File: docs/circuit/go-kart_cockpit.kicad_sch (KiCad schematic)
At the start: 21 parts, among them J1 2x13, J2 2x13, Q1 TIP120, SW1 SW_MEC_5E, X1 AVR-ISP-10, X2 Display (2x3 male), X3 24V Hupe, X4 Start/Stop/Rückwärts, X5 Bluetooth-Modul, X6 Taster rechts (2x5 male), X7 Taster links (male)

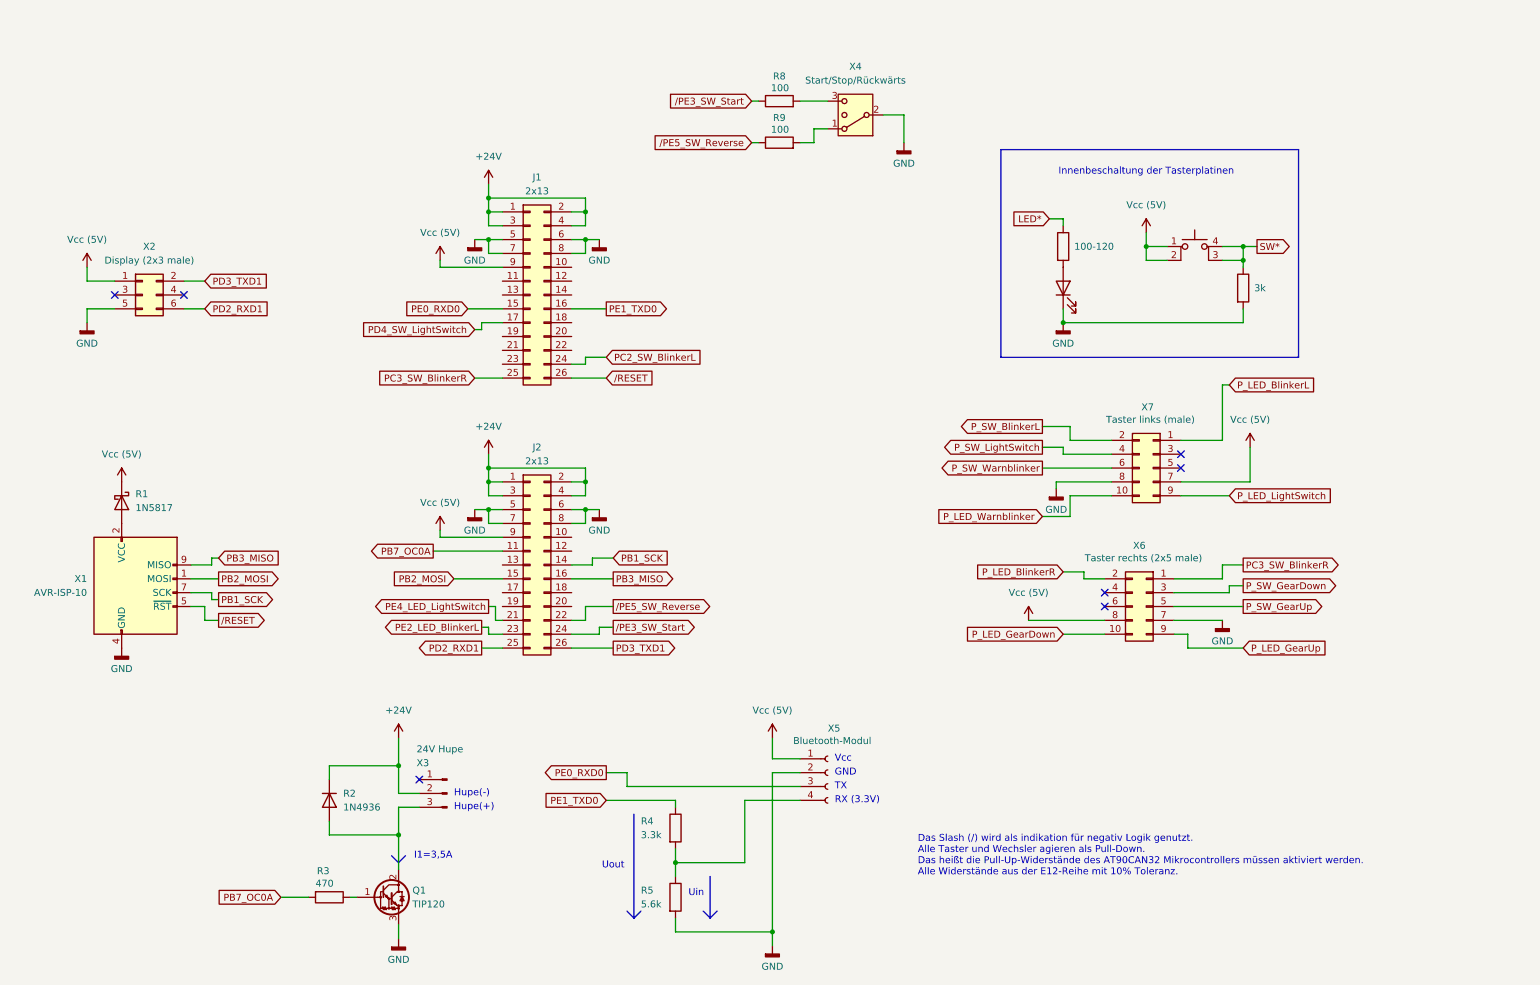
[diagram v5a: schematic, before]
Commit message: feat: planned connections to MCU
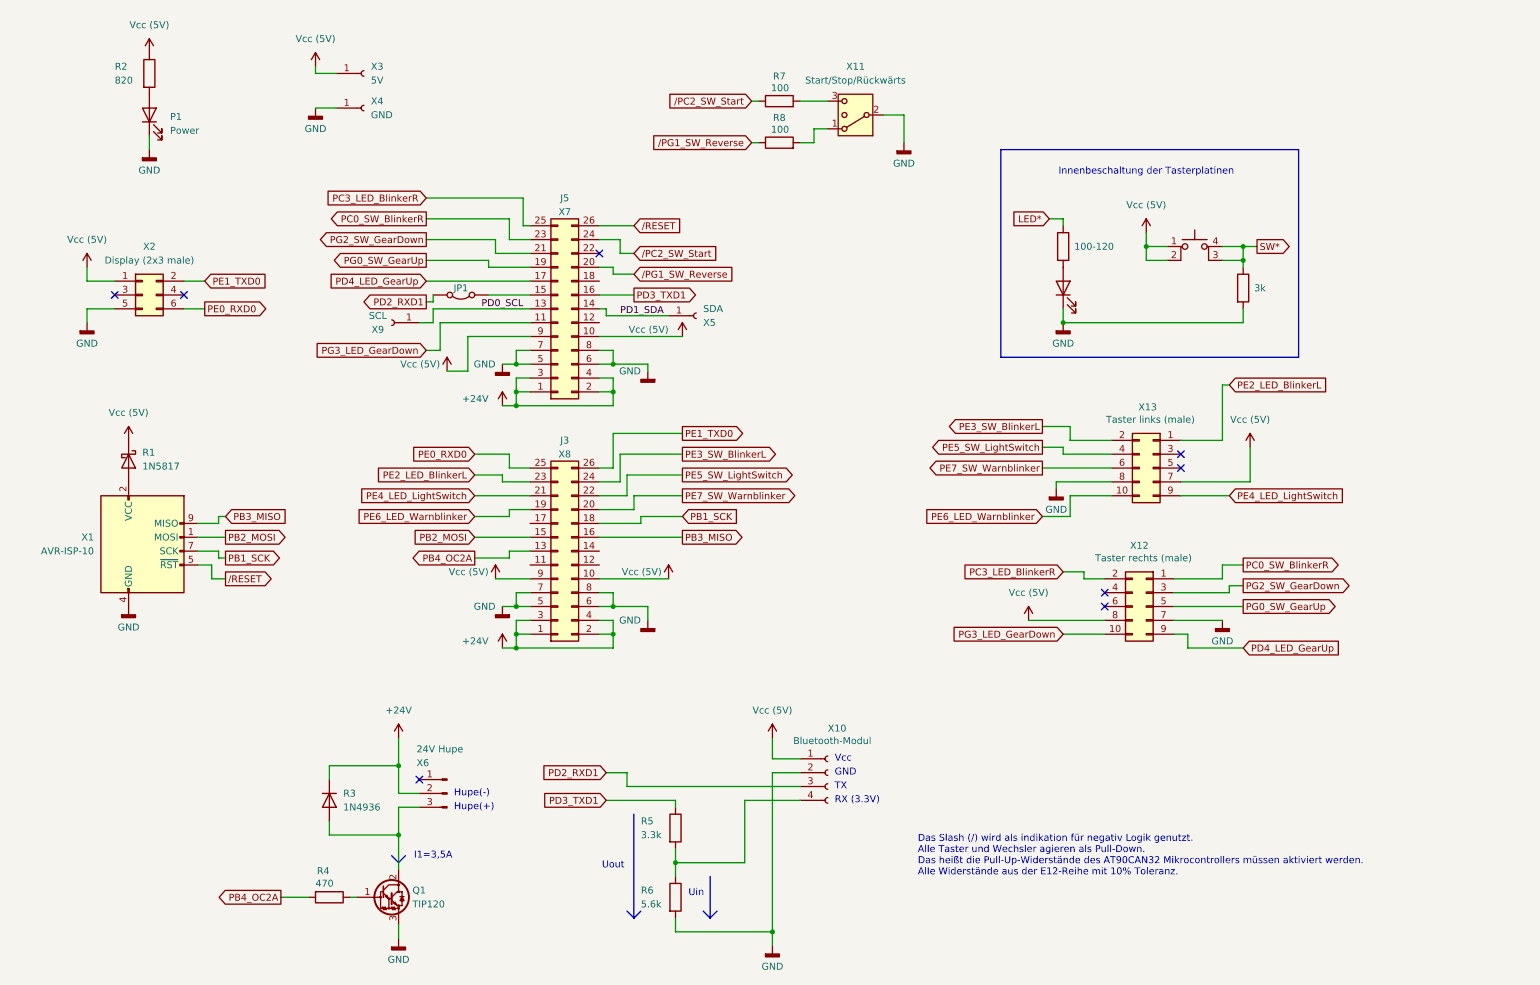
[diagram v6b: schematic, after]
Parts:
- added JP1: ~, Library:Bridge, symbol Jumper:Jumper_2_Bridged
- added P1: Power, LED_THT:LED_D5.0mm_Horizontal_O3.81mm_Z15.0mm, symbol Device:LED
- added R2: 820, Resistor_THT:R_Axial_DIN0204_L3.6mm_D1.6mm_P7.62mm_Horizontal, symbol Device:R
- added X3: 5V, Connector_PinHeader_2.54mm:PinHeader_1x01_P2.54mm_Vertical, symbol Connector:Conn_01x01_Socket
- added X4: GND, Connector_PinHeader_2.54mm:PinHeader_1x01_P2.54mm_Vertical, symbol Connector:Conn_01x01_Socket
- added X5: SDA, Connector_PinHeader_2.54mm:PinHeader_1x01_P2.54mm_Vertical, symbol Connector:Conn_01x01_Socket
- added X9: SCL, Connector_PinHeader_2.54mm:PinHeader_1x01_P2.54mm_Vertical, symbol Connector:Conn_01x01_Socket
- Q1: footprint Package_TO_SOT_THT:TO-220F-3_Horizontal_TabDown -> Package_TO_SOT_THT:TO-220-3_Horizontal_TabDown
- X11: renamed from X4; footprint TerminalBlock_Phoenix:TerminalBlock_Phoenix_MKDS-1,5-3-5.08_1x03_P5.08mm_Horizontal -> Library:Elecbee_3pin_Green_Connector_1.5mm
- X12: renamed from X6; value Taster rechts (2x5 male) -> Taster rechts (male)
- X6: renamed from X3; footprint TerminalBlock_Phoenix:TerminalBlock_Phoenix_MKDS-1,5-3-5.08_1x03_P5.08mm_Horizontal -> Library:Elecbee_3pin_Green_Connector_1.5mm
- X7: renamed from J1; value 2x13 -> J5
- X8: renamed from J2; value 2x13 -> J3
- renumbered R7 to R10, R2 to R3, R3 to R4, R4 to R5, R5 to R6, R8 to R7, R9 to R8, R6 to R9, X5 to X10, X7 to X13
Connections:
- net P_LED_BlinkerL is gone; now on net PE2_LED_BlinkerL: X13.1 (Pin_1)
- net P_LED_BlinkerR is gone; now on net PC3_LED_BlinkerR: X12.2 (Pin_2)
- net P_LED_GearDown is gone; now on net PG3_LED_GearDown: X12.10 (Pin_10)
- net P_LED_GearUp is gone; now on net PD4_LED_GearUp: X12.9 (Pin_9)
- net P_LED_LightSwitch is gone; now on net PE4_LED_LightSwitch: X13.9 (Pin_9)
- net P_LED_Warnblinker is gone; now on net PE6_LED_Warnblinker: X13.10 (Pin_10)
- net P_SW_GearDown is gone; now on net PG2_SW_GearDown: X12.3 (Pin_3)
- net P_SW_GearUp is gone; now on net PG0_SW_GearUp: X12.5 (Pin_5)
- net P_SW_Warnblinker is gone; now on net PE7_SW_Warnblinker: X13.6 (Pin_6)
- net GND: now also P1.1 (K), X4.1 (Pin_1)
- net PB1_SCK: now also X8.18 (Pin_18); no longer X8.14 (Pin_14)
- net PD2_RXD1: now also X10.3 (Pin_3), JP1.1 (A); no longer X2.6 (Pin_6), X8.25 (Pin_25)
- net PD3_TXD1: now also R5.1, X7.16 (Pin_16); no longer X2.2 (Pin_2), X8.26 (Pin_26)
- net PE0_RXD0: now also X2.6 (Pin_6), X8.25 (Pin_25); no longer X10.3 (Pin_3), X7.15 (Pin_15)
- net PE1_TXD0: now also X2.2 (Pin_2), X8.26 (Pin_26); no longer R5.1, X7.16 (Pin_16)
- net Vcc (5V): now also X7.10 (Pin_10), X8.10 (Pin_10), R2.1, X3.1 (Pin_1)
- net PG3_LED_GearDown: now reaches X7.11 (Pin_11)
- net PD0_SCL: now reaches X7.13 (Pin_13)
- net PD0_SCL: now also X9.1 (Pin_1)
- net PD1_SDA: now reaches X7.14 (Pin_14)
- net PD1_SDA: now also X5.1 (Pin_1)
- net PG0_SW_GearUp: now reaches X7.19 (Pin_19)
- net /PG1_SW_Reverse: now reaches X7.20 (Pin_20)
- net /PG1_SW_Reverse: now also R8.1
- net PG2_SW_GearDown: now reaches X7.21 (Pin_21)
- net PC0_SW_BlinkerR: now reaches X7.23 (Pin_23)
- net PC0_SW_BlinkerR: now also X12.1 (Pin_1)
- net PB4_OC2A: now reaches X8.13 (Pin_13)
- net PB4_OC2A: now also R4.2
- net PE6_LED_Warnblinker: now reaches X8.19 (Pin_19)
- net PE7_SW_Warnblinker: now reaches X8.20 (Pin_20)
- net PB7_OC0A: no longer names the net of X8.11 (Pin_11)
- net PB7_OC0A: no longer R4.2
- net PC2_SW_BlinkerL renamed /PC2_SW_Start
- net /PC2_SW_Start: now also R7.1
- net PC3_SW_BlinkerR renamed PC3_LED_BlinkerR
- net PC3_LED_BlinkerR: no longer X12.1 (Pin_1)
- net PD4_SW_LightSwitch renamed PD4_LED_GearUp
- net P_SW_BlinkerL renamed PE3_SW_BlinkerL
- net PE3_SW_BlinkerL: now also X8.24 (Pin_24)
- net P_SW_LightSwitch renamed PE5_SW_LightSwitch
- net PE5_SW_LightSwitch: now also X8.22 (Pin_22)
- removed net /PE3_SW_Start: R7.1, X8.24 (Pin_24)
- removed net /PE5_SW_Reverse: R8.1, X8.22 (Pin_22)
- new net: JP1.2 (B), X7.15 (Pin_15)
- new net: P1.2 (A), R2.2
- no-connect marks 7 -> 8
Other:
- moved on the sheet: R1, X1, X7, X8
